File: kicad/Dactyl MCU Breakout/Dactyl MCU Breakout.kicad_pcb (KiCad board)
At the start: 4 copper layers, 99.4 x 61.1 mm, 74 parts, among them J201 JST, J202 Split, J203 Column, J204 Thumb, J205 External, J206 Row, J207 Display, J208 Vic, J301 JST, J302 Split, J303 Column, J304 Thumb, J305 External, J306 Row, J307 Display, J308 Vic, SW201 Battery, SW202 Reset, SW203 LED, SW301 Battery, SW302 Reset, SW303 LED, U201 SRV05-4, U202 Nice!Nano/2040, U301 SRV05-4, U302 Nice!Nano/2040

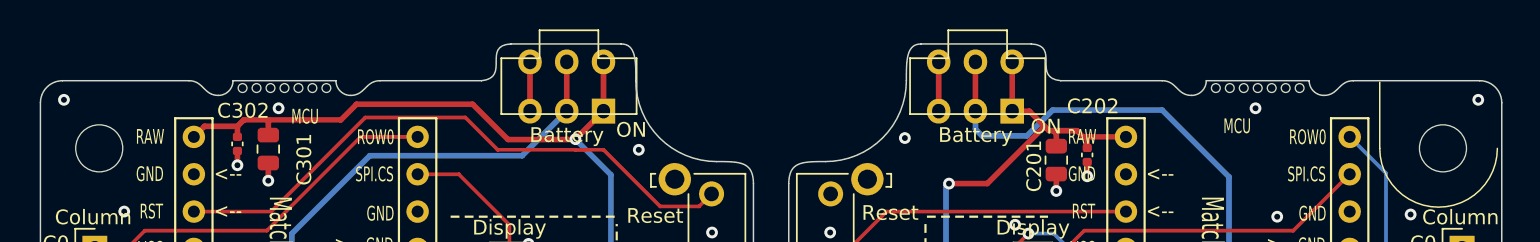
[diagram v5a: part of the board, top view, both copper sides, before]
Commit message: feat(pcb): put breaks for panel at whole mm's
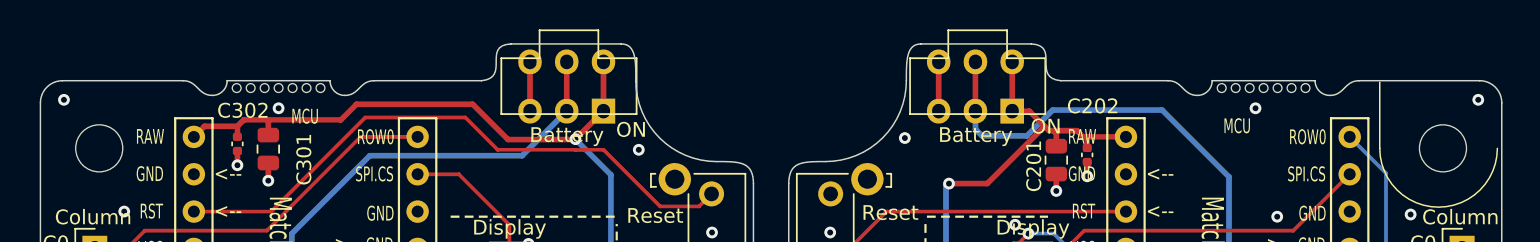
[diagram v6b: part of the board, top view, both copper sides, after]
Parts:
- moved REF** 0.40 mm to (66.0, 50.5)
- moved REF** 0.40 mm to (133.0, 50.5)
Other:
- outline, holes or cut-outs redrawn
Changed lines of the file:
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@@
 		(tags "resistor")
 		(property "Reference" "R301"
-			(at 3.4 0 360)
+			(at 3.4 0 0)
 			(layer "F.SilkS")
 			(effects
@@
 		)
 		(property "Value" "300 Ohm"
-			(at -1.9 1.43 360)
+			(at -1.9 1.43 0)
 			(layer "F.Fab")
 			(effects
@@
 		)
 		(fp_text user "${REFERENCE}"
-			(at 0 0 360)
+			(at 0 0 0)
 			(layer "F.Fab")
 			(effects
@@
 		(fp_arc
 			(start 6.938123 15.132041)
-			(mid 6.337066 14.8831)
+			(mid 6.337062 14.8831)
 			(end 6.088123 14.282041)
 			(stroke
@@
 		(fp_arc
 			(start 8.236041 -15.740877)
-			(mid 8.837089 -15.491924)
+			(mid 8.837086 -15.491923)
 			(end 9.086041 -14.890877)
 			(stroke
@@
 		(fp_arc
 			(start 6.938123 15.132041)
-			(mid 6.337066 14.8831)
+			(mid 6.337062 14.8831)
 			(end 6.088123 14.282041)
 			(stroke
@@
 		(fp_arc
 			(start 8.236041 -15.740877)
-			(mid 8.837089 -15.491924)
+			(mid 8.837086 -15.491923)
 			(end 9.086041 -14.890877)
 			(stroke
@@
 	(footprint "Dactyl_basics:Mouse_Bites"
 		(layer "F.Cu")
-		(at 66.4 50.5)
+		(at 66 50.5)
 		(property "Reference" "REF**"
 			(at 0 9.4 0)
@@
 	(footprint "Dactyl_basics:Mouse_Bites"
 		(layer "F.Cu")
-		(at 132.6 50.5)
+		(at 133 50.5)
 		(property "Reference" "REF**"
 			(at 0 9.4 0)
@@
 	(gr_curve
 		(pts
-			(xy 59.9 50) (xy 60.9 50) (xy 60.9 51) (xy 61.9 51)
+			(xy 59.5 50) (xy 60.5 50) (xy 60.5 51) (xy 61.5 51)
 		)
 		(stroke
@@
 	(gr_curve
 		(pts
-			(xy 72.9 50) (xy 71.9 50) (xy 71.9 51) (xy 70.9 51)
+			(xy 72.5 50) (xy 71.5 50) (xy 71.5 51) (xy 70.5 51)
 		)
 		(stroke
@@
 	(gr_line
 		(start 119.2 50)
-		(end 126.1 50)
+		(end 126.5 50)
 		(stroke
 			(width 0.1)
@@
 	)
 	(gr_line
-		(start 129.1 50)
-		(end 136.1 50)
+		(start 129.5 50)
+		(end 136.5 50)
 		(stroke
 			(width 0.1)
@@
 	)
 	(gr_arc
-		(start 129.1 50)
-		(mid 128.807107 50.707107)
-		(end 128.1 51)
+		(start 129.5 50)
+		(mid 129.207107 50.707107)
+		(end 128.5 51)
 		(stroke
 			(width 0.1)
@@
 	)
 	(gr_arc
-		(start 62.9 50)
-		(mid 62.607107 50.707107)
-		(end 61.9 51)
+		(start 62.5 50)
+		(mid 62.207107 50.707107)
+		(end 61.5 51)
 		(stroke
 			(width 0.1)
@@
 	)
 	(gr_line
-		(start 62.9 50)
-		(end 69.9 50)
+		(start 62.5 50)
+		(end 69.5 50)
 		(stroke
 			(width 0.1)
@@
 	)
 	(gr_line
-		(start 72.9 50)
+		(start 72.5 50)
 		(end 79.8 50)
 		(stroke
@@
 	(gr_curve
 		(pts
-			(xy 139.1 50) (xy 138.1 50) (xy 138.1 51) (xy 137.1 51)
+			(xy 139.5 50) (xy 138.5 50) (xy 138.5 51) (xy 137.5 51)
 		)
 		(stroke
@@
 	(gr_line
 		(start 51.3 50)
-		(end 59.9 50)
+		(end 59.5 50)
 		(stroke
 			(width 0.1)
@@
 	(gr_curve
 		(pts
-			(xy 126.1 50) (xy 127.1 50) (xy 127.1 51) (xy 128.1 51)
+			(xy 126.5 50) (xy 127.5 50) (xy 127.5 51) (xy 128.5 51)
 		)
 		(stroke
@@
 	)
 	(gr_line
-		(start 139.1 50)
+		(start 139.5 50)
 		(end 147.7 50)
 		(stroke
@@
 	)
 	(gr_arc
-		(start 137.1 51)
-		(mid 136.392893 50.707107)
-		(end 136.1 50)
+		(start 137.5 51)
+		(mid 136.792893 50.707107)
+		(end 136.5 50)
 		(stroke
 			(width 0.1)
@@
 	)
 	(gr_arc
-		(start 70.9 51)
-		(mid 70.192893 50.707107)
-		(end 69.9 50)
+		(start 70.5 51)
+		(mid 69.792893 50.707107)
+		(end 69.5 50)
 		(stroke
 			(width 0.1)
@@
 	)
 	(gr_line
-		(start 99.5 47)
+		(start 99.5 40)
 		(end 99.5 53)
 		(stroke
@@
 	)
 	(gr_text "Space for\nbottom plate\nsupport shelf"
-		(at 108.3 41.1 0)
+		(at 166.9 39 0)
 		(layer "User.9")
 		(effects
@@
 	)
 	(gr_text "Grid origin\nso mirroring\nx is easier"
-		(at 96.6 39.1 0)
+		(at 89.7 31.3 0)
 		(layer "User.9")
 		(effects
@@
 	)
 	(gr_text_box "A grid of .1 mm is used for components that interface with the case.\nThis is to make it easier to maintain left and right board consistency.\nThis includes:\n\n- Board outline\n- Through case componentes including MCU\n- Mount holes\n- LEDs"
-		(start 86.5 120)
-		(end 120.9 140.075)
+		(start 82.1 121.7)
+		(end 116.5 141.775)
 		(layer "User.9")
 		(effects
@@
 		(layer "User.9")
 		(pts
-			(xy 61.163298 106.4) (xy 55.663298 106.4)
-		)
-		(height -3.5)
-		(gr_text "5.5 mm"
-			(at 60.463298 111.5 0)
-			(layer "User.9")
-			(effects
-				(font
-					(size 1 1)
-					(thickness 0.15)
-				)
-			)
-		)
-		(format
-			(prefix "")
-			(suffix "")
-			(units 3)
-			(units_format 1)
-			(precision 1)
-		)
-		(style
-			(thickness 0.15)
-			(arrow_length 1.27)
-			(text_position_mode 2)
-			(extension_height 0.58642)
-			(extension_offset 0.5) keep_text_aligned)
-	)
-	(dimension
-		(type aligned)
-		(layer "User.9")
-		(pts
 			(xy 108.5 50) (xy 103 50)
 		)
-		(height 3.5)
+		(height 1)
 		(gr_text "5.5 mm"
-			(at 107.8 44.9 0)
+			(at 105.5 51 0)
 			(layer "User.9")
 			(effects
@@
 		(polygon
 			(pts
-				(xy 9.5 10) (xy 9.5 206) (xy 99 206) (xy 99 10)
+				(xy 46.5 46) (xy 46.5 110) (xy 99 110) (xy 99 46)
 			)
 		)
@@
 		(polygon
 			(pts
-				(xy 100 10) (xy 100 206) (xy 192 206) (xy 192 10)
+				(xy 100 46) (xy 100 110) (xy 152 110) (xy 152 46)
 			)
 		)

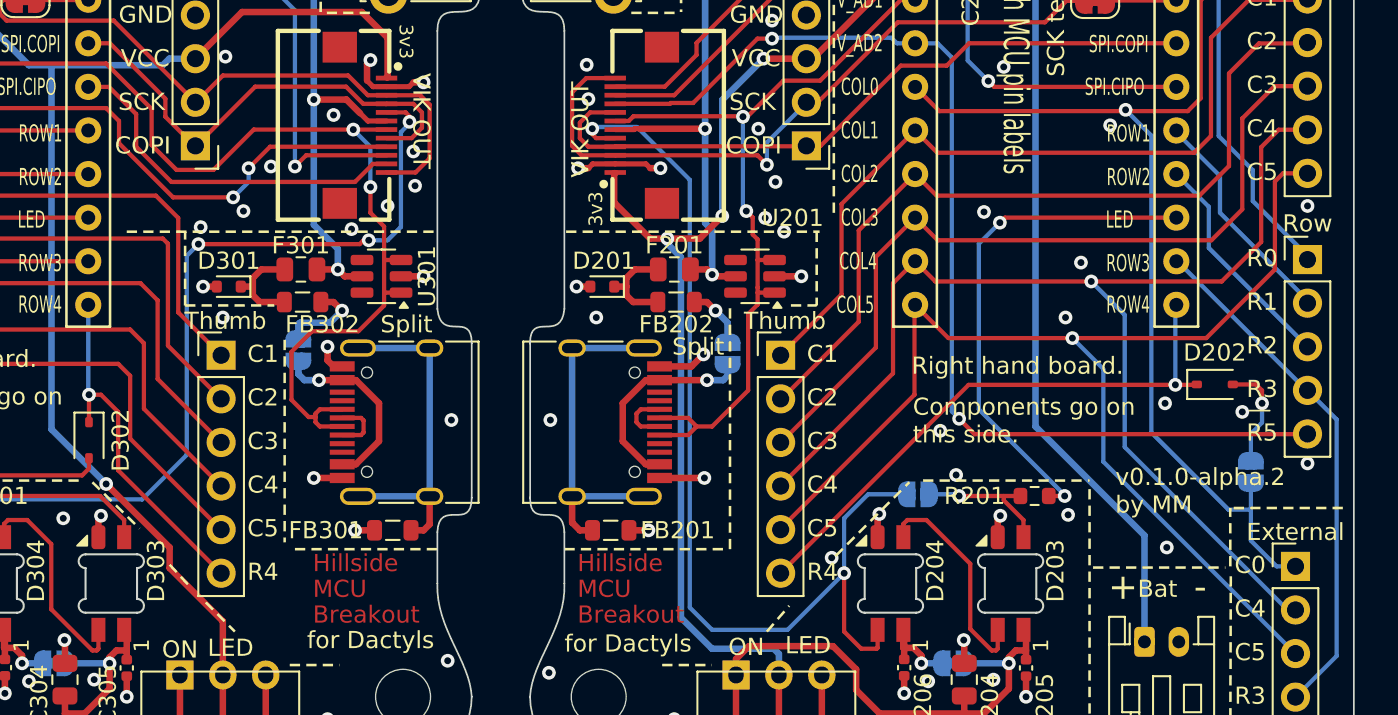
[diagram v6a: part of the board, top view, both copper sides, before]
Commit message: feat: handedness jumper only on left board
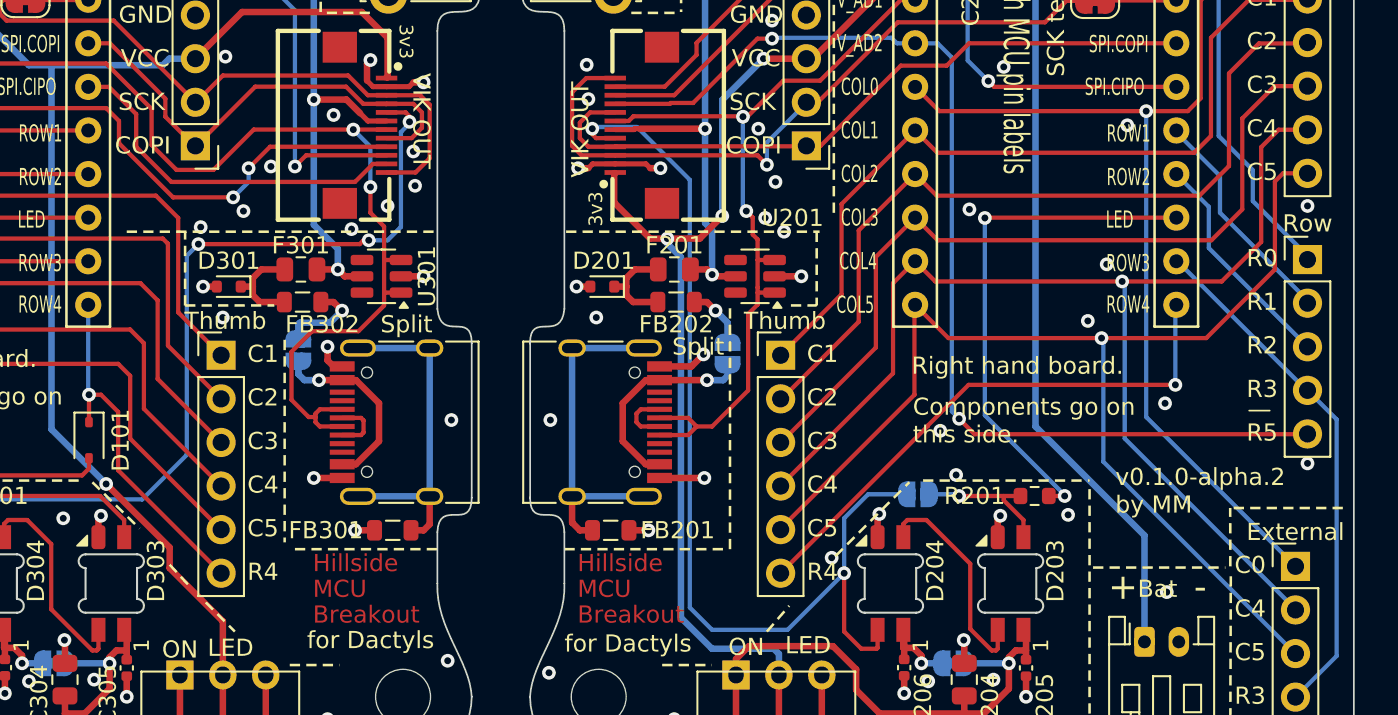
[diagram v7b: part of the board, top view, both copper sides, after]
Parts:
- removed D202: D_Small, Diode_SMD:D_SOD-323
- removed JP202: Wired Left, Dactyl_basics:SolderJumper-2_P1.3mm_Open_RoundedPad1.0x1.5mm
- renumbered D302 to D101, JP302 to JP101
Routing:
- net Net-(D202-A): track 6.24 -> 0.00 mm, vias 1 -> 0
- net /Right/col0: track 64.2 -> 60.7 mm
- net /Right/row4: track 33.5 -> 32.2 mm
- net /Right/col4: track 70.9 -> 69.9 mm
- net /Right/col5: track 70.8 -> 70.1 mm
- net /Right/GND: vias 52 -> 51

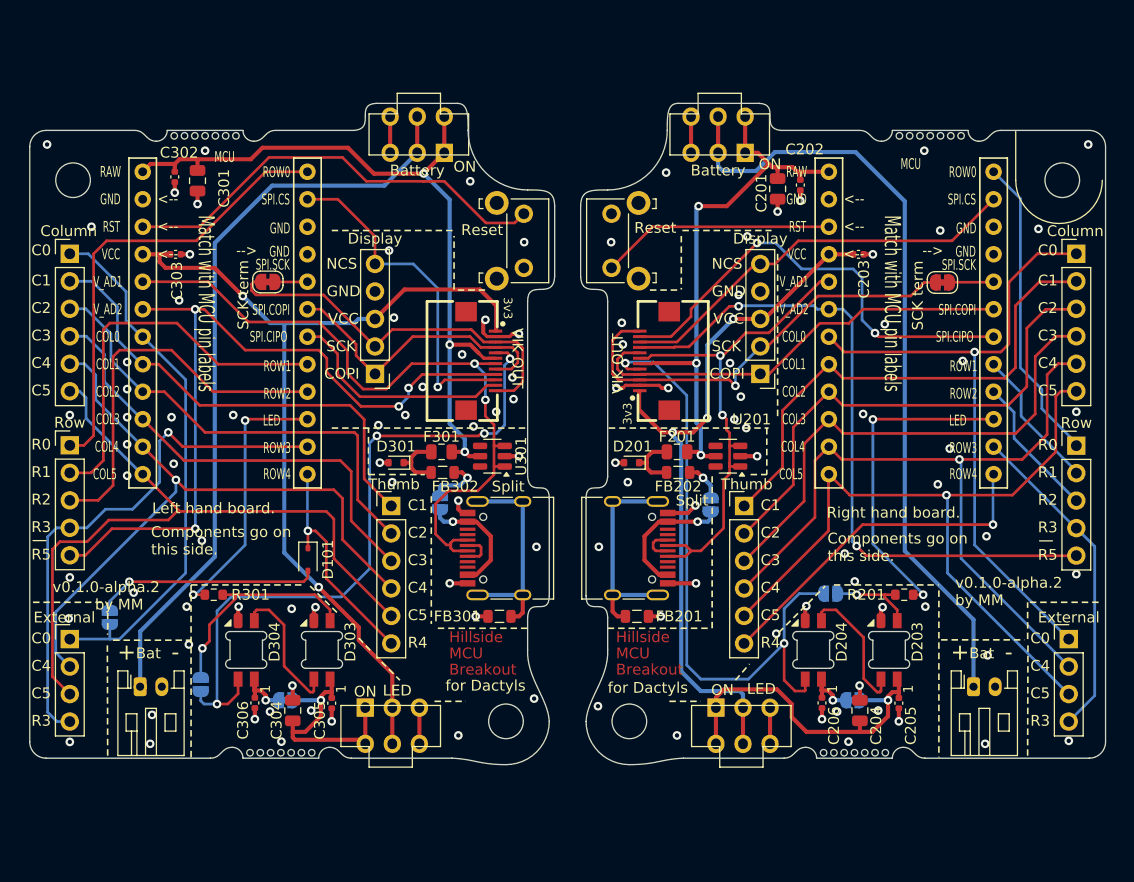
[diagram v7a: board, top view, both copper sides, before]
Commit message: feat(pcb): add rails around breakout boards
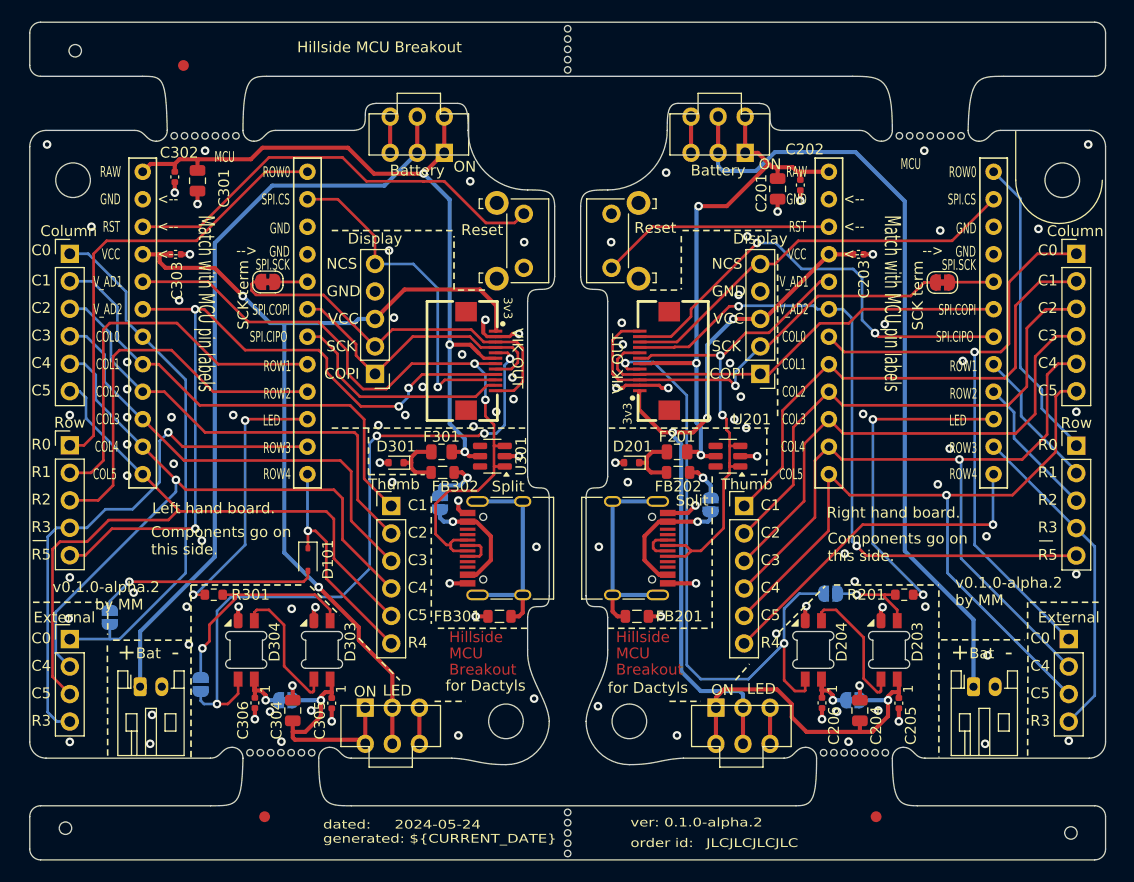
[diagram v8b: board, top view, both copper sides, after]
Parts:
- added FID1: Fiducial, Fiducial:Fiducial_1mm_Mask2mm, F.Cu at (64.0, 44.0)
- added FID2: Fiducial, Fiducial:Fiducial_1mm_Mask2mm, F.Cu at (71.5, 113.4)
- added FID3: Fiducial, Fiducial:Fiducial_1mm_Mask2mm, F.Cu at (128.0, 113.4)
- added H3: ToolingHole, Dactyl:ToolingHole_1.152mm, F.Cu at (54.0, 42.6)
- added H4: ToolingHole, Dactyl:ToolingHole_1.152mm, F.Cu at (53.1, 114.5)
- added H5: ToolingHole, Dactyl:ToolingHole_1.152mm, F.Cu at (146.0, 114.9)
- added REF**: Mouse_Bites_5mm, Dactyl:Mouse_Bites_5mm, F.Cu at (99.5, 114.9)
- added REF**: Mouse_Bites_5mm, Dactyl:Mouse_Bites_5mm, F.Cu at (99.5, 42.5)
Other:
- board size 99.4 x 61.1 mm -> 99.4 x 77.4 mm
- board text added: "${TITLE}"
- board text added: "JLCJLCJLCJLC"
- board text added: "dated: ${ISSUE_DATE} generated: ${CURRENT_DATE}"
- board text added: "order id:"
- board text added: "ver: ${REVISION}"
